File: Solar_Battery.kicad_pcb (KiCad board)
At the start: 2 copper layers, 1 part, among them U1 UCC28710DR

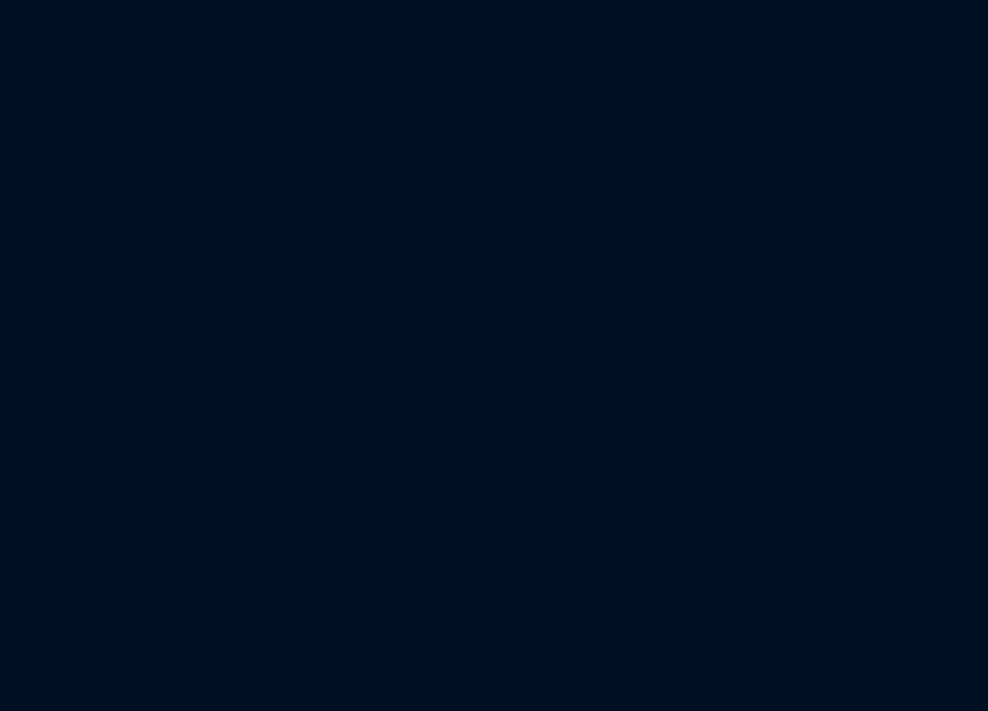
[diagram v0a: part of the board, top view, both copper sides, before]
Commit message: BQ Chip Symbol & Footprint
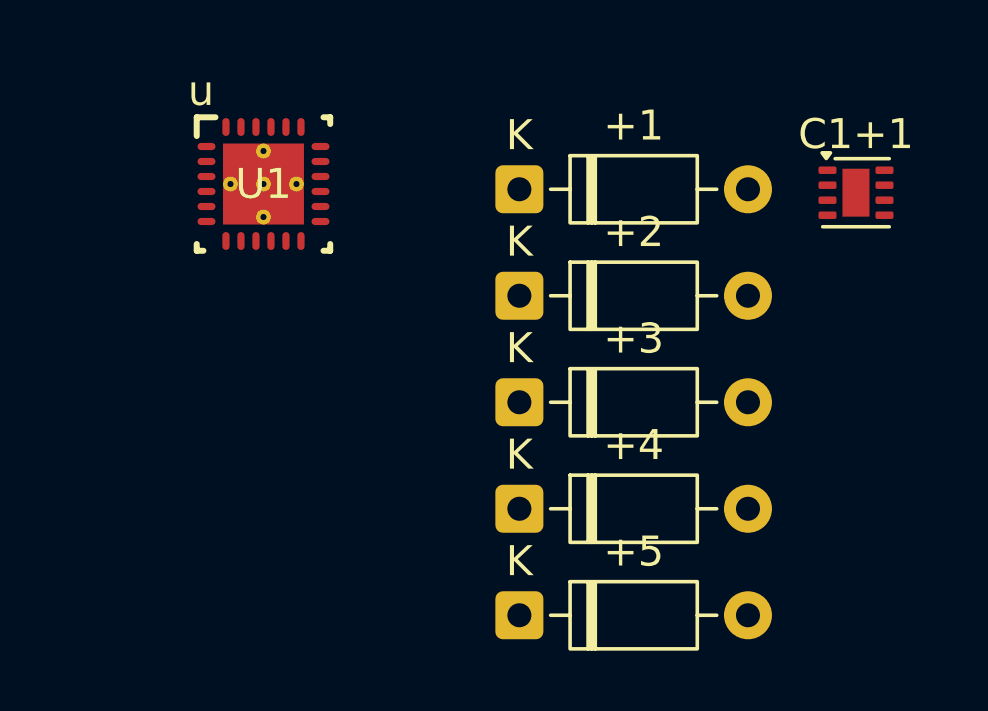
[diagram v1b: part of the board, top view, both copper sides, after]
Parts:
- added +1: RSNUB2, Diode_THT:D_DO-35_SOD27_P7.62mm_Horizontal, F.Cu at (116.5, 73.8)
- added +2: DSNUB, Diode_THT:D_DO-35_SOD27_P7.62mm_Horizontal, F.Cu at (116.5, 77.3)
- added +3: RSNUB1, Diode_THT:D_DO-35_SOD27_P7.62mm_Horizontal, F.Cu at (116.5, 80.9)
- added +4: D2-ZENER, Diode_THT:D_DO-35_SOD27_P7.62mm_Horizontal, F.Cu at (116.5, 84.4)
- added +5: RLBD, Diode_THT:D_DO-35_SOD27_P7.62mm_Horizontal, F.Cu at (116.5, 88.0)
- added C1+1: C, Package_SON:Texas_DSG0008A_WSON-8-1EP_2x2mm_P0.5mm_EP0.9x1.6mm, F.Cu at (127.8, 73.9)
- added U1: BQ25895RTWR, BQ:RTW0024H, F.Cu at (108.0, 73.6)

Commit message: change
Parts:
- added +10: DZ-ZENER, Diode_THT:D_DO-35_SOD27_P7.62mm_Horizontal, F.Cu at (14.4, 42.0)
- added +11: RDD, Resistor_THT:R_Axial_DIN0207_L6.3mm_D2.5mm_P10.16mm_Horizontal, F.Cu at (1.07, 52.1)
- added +12: D3-ZENER, Diode_THT:D_DO-35_SOD27_P7.62mm_Horizontal, F.Cu at (14.4, 45.5)
- added +13: RFBB, Resistor_THT:R_Axial_DIN0207_L6.3mm_D2.5mm_P10.16mm_Horizontal, F.Cu at (1.07, 56.2)
- added +14: RFBT, Resistor_THT:R_Axial_DIN0207_L6.3mm_D2.5mm_P10.16mm_Horizontal, F.Cu at (1.07, 60.2)
- added +6: RG2, Resistor_THT:R_Axial_DIN0207_L6.3mm_D2.5mm_P10.16mm_Horizontal, F.Cu at (1.07, 35.9)
- added +7: RG1, Resistor_THT:R_Axial_DIN0207_L6.3mm_D2.5mm_P10.16mm_Horizontal, F.Cu at (1.07, 40.0)
- added +8: RLC, Resistor_THT:R_Axial_DIN0207_L6.3mm_D2.5mm_P10.16mm_Horizontal, F.Cu at (1.07, 44.0)
- added +9: RCS, Resistor_THT:R_Axial_DIN0207_L6.3mm_D2.5mm_P10.16mm_Horizontal, F.Cu at (1.07, 48.1)
- added BT1: Battery_Cell, Package_SO:SOIC-20W_7.5x12.8mm_P1.27mm, F.Cu at (25.8, 6.81)
- added C1: 40µF, Capacitor_THT:C_Disc_D5.0mm_W2.5mm_P2.50mm, F.Cu at (14.8, 1.52)
- added C2: 1µF, Capacitor_THT:C_Disc_D5.0mm_W2.5mm_P2.50mm, F.Cu at (14.8, 5.58)
- added C3: 47nF, Capacitor_THT:C_Disc_D5.0mm_W2.5mm_P2.50mm, F.Cu at (14.8, 9.62)
- added C4: 4.7µF, Capacitor_THT:C_Disc_D5.0mm_W2.5mm_P2.50mm, F.Cu at (14.8, 13.7)
- added C5: 10µF, Capacitor_THT:C_Disc_D5.0mm_W2.5mm_P2.50mm, F.Cu at (14.8, 17.7)
- added C6: 10µF, Capacitor_THT:C_Disc_D5.0mm_W2.5mm_P2.50mm, F.Cu at (14.8, 21.8)
- added C7: 10uF, Capacitor_THT:C_Disc_D5.0mm_W2.5mm_P2.50mm, F.Cu at (14.8, 25.8)
- added CDD1: +, Package_SO:SOIC-8_3.9x4.9mm_P1.27mm, F.Cu at (17.0, 57.3)
- added CSNUB1: +, Capacitor_THT:C_Disc_D5.0mm_W2.5mm_P2.50mm, F.Cu at (36.3, 1.52)
- added Cin1: 4.237uF, Capacitor_THT:C_Disc_D10.0mm_W2.5mm_P5.00mm, F.Cu at (32.0, 58.1)
- added Cin2: 4.237uF, Capacitor_THT:C_Disc_D10.0mm_W2.5mm_P5.00mm, F.Cu at (32.0, 62.2)
- added D1: LED_1, OptoDevice:R_LDR_D6.4mm_P3.4mm_Vertical, F.Cu at (21.7, 18.0)
- added Dac1: D, Diode_THT:D_DO-201AD_P15.24mm_Horizontal, F.Cu at (31.1, 37.3)
- added Dac2: D, Diode_THT:D_DO-15_P15.24mm_Horizontal, F.Cu at (30.7, 43.2)
- added Dac3: D, Diode_THT:D_DO-15_P15.24mm_Horizontal, F.Cu at (30.7, 48.4)
- added Dac4: D, Diode_THT:D_DO-15_P15.24mm_Horizontal, F.Cu at (30.7, 53.5)
- added L1: 2.2µH, Inductor_SMD:L_CommonModeChoke_Coilcraft_0603USB, F.Cu at (20.6, 29.2)
- added L2: 470uH, Inductor_THT:L_Axial_L6.6mm_D2.7mm_P2.54mm_Vertical_Vishay_IM-2, F.Cu at (50.1, 42.8)
- added R1: 10kΩ, Resistor_THT:R_Axial_DIN0207_L6.3mm_D2.5mm_P10.16mm_Horizontal, F.Cu at (1.07, 1.52)
- added R2: 10kΩ, Resistor_THT:R_Axial_DIN0207_L6.3mm_D2.5mm_P10.16mm_Horizontal, F.Cu at (1.07, 5.58)
- added R3: 10kΩ, Resistor_THT:R_Axial_DIN0207_L6.3mm_D2.5mm_P10.16mm_Horizontal, F.Cu at (1.07, 9.62)
- added R4: 260Ω, Resistor_THT:R_Axial_DIN0207_L6.3mm_D2.5mm_P10.16mm_Horizontal, F.Cu at (1.07, 13.7)
- added R5: 2.2KΩ, Resistor_THT:R_Axial_DIN0207_L6.3mm_D2.5mm_P10.16mm_Horizontal, F.Cu at (1.07, 17.7)
- added R6: 5.23KΩ, Resistor_THT:R_Axial_DIN0207_L6.3mm_D2.5mm_P10.16mm_Horizontal, F.Cu at (1.07, 21.8)
- added R7: 30.1KΩ, Resistor_THT:R_Axial_DIN0207_L6.3mm_D2.5mm_P10.16mm_Horizontal, F.Cu at (1.07, 25.8)
- added R8: 10KΩ, Resistor_THT:R_Axial_DIN0207_L6.3mm_D2.5mm_P10.16mm_Horizontal, F.Cu at (1.07, 29.9)
- added Rl1: 13 ohm, Resistor_THT:R_Axial_DIN0207_L6.3mm_D2.5mm_P7.62mm_Horizontal, F.Cu at (41.9, 58.1)
- added SW1: SW_Push, Button_Switch_SMD:SW_SPST_CK_KMS2xxGP, F.Cu at (22.6, 24.5)
- added T1: T1, Transformer_THT:Transformer_Toroid_Tapped_Horizontal_D10.5mm_Amidon-T37, F.Cu at (192.3, 51.8)
- added U2: IRF830APBF, footprints:TO220AB_VIS, F.Cu at (18.0, 37.1)
- added U3: UCC28710DR, footprints:SO_UCC28710D_TEX, F.Cu at (17.1, 50.6)
- C1+1: footprint Package_SON:Texas_DSG0008A_WSON-8-1EP_2x2mm_P0.5mm_EP0.9x1.6mm -> Capacitor_THT:C_Disc_D5.0mm_W2.5mm_P2.50mm
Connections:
- net Net-(+4-K) renamed /Rectifier/Transformer_Output/Main_Output
- net Net-(T1-AA) renamed /Rectifier/Transformer_Output/Rectifier_GND
- +2 pad 2: Net-(+2-A) -> /Rectifier/Transformer_Output/Mosfet_Snub
- +3 pad 1: Net-(T1-SA) -> /Rectifier/Diode_Bridge/Rectifier_Out
- U1 pad 1: unconnected-(U1-VBUS-Pad1) -> Earth
- U1 pad 10: unconnected-(U1-ILIM-Pad10) -> Net-(U1-ILIM)
- U1 pad 11: unconnected-(U1-TS-Pad11) -> Net-(U1-TS)
- U1 pad 12: unconnected-(U1-QON_N-Pad12) -> Net-(U1-QON_N)
- U1 pad 14: unconnected-(U1-BAT-Pad14) -> Net-(BT1-+)
- U1 pad 15: unconnected-(U1-SYS-Pad15) -> /Battery_Controller/SYS?
- U1 pad 17: unconnected-(U1-PGND-Pad17) -> Earth
- U1 pad 19: unconnected-(U1-SW-Pad19) -> Net-(C3-Pad2)
- U1 pad 2: unconnected-(U1-D+-Pad2) -> Earth
- U1 pad 21: unconnected-(U1-BTST-Pad21) -> Net-(U1-BTST)
- U1 pad 22: unconnected-(U1-REGN-Pad22) -> Net-(U1-REGN)
- U1 pad 23: unconnected-(U1-PMID-Pad23) -> /Battery_Controller/Phone
- U1 pad 24: unconnected-(U1-DSEL-Pad24) -> /Battery_Controller/NOT IN DIAGRAM
- U1 pad 25: unconnected-(U1-PAD-Pad25) -> /Battery_Controller/NOT IN DIAGRAM
- U1 pad 3: unconnected-(U1-D--Pad3) -> Earth
- U1 pad 4: unconnected-(U1-STAT-Pad4) -> Net-(U1-STAT)
- U1 pad 5: unconnected-(U1-SCL-Pad5) -> /Battery_Controller/Host
- U1 pad 6: unconnected-(U1-SDA-Pad6) -> /Battery_Controller/Host
- U1 pad 7: unconnected-(U1-INT-Pad7) -> /Battery_Controller/Host
- U1 pad 8: unconnected-(U1-OTG-Pad8) -> /Battery_Controller/Host
- U1 pad 9: unconnected-(U1-CE_N-Pad9) -> /Battery_Controller/Host

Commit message: change
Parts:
- moved R1 236.2 mm to (208.8, 113.8)
- moved R2 236.2 mm to (208.8, 117.9)
- moved R3 236.2 mm to (208.8, 122.0)
- moved R4 236.2 mm to (208.8, 126.0)
- moved R5 236.2 mm to (208.8, 130.1)
- moved R6 236.2 mm to (208.8, 134.1)
- moved R7 236.2 mm to (208.8, 138.2)
- moved R8 236.2 mm to (208.8, 142.2)
- moved C1 236.2 mm to (222.6, 113.8)
- moved +6 129.4 mm to (97.4, 122.3)
- moved +7 129.4 mm to (97.4, 126.3)
- moved +8 129.4 mm to (97.4, 130.4)
- moved +9 129.4 mm to (97.4, 134.4)
- moved +13 129.0 mm to (96.9, 142.6)
- moved +11 129.0 mm to (96.9, 138.5)
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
